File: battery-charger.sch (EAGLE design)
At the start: 9 parts, among them J2 10118192-0001LF, U1 MCP73831T-2DCI/OT

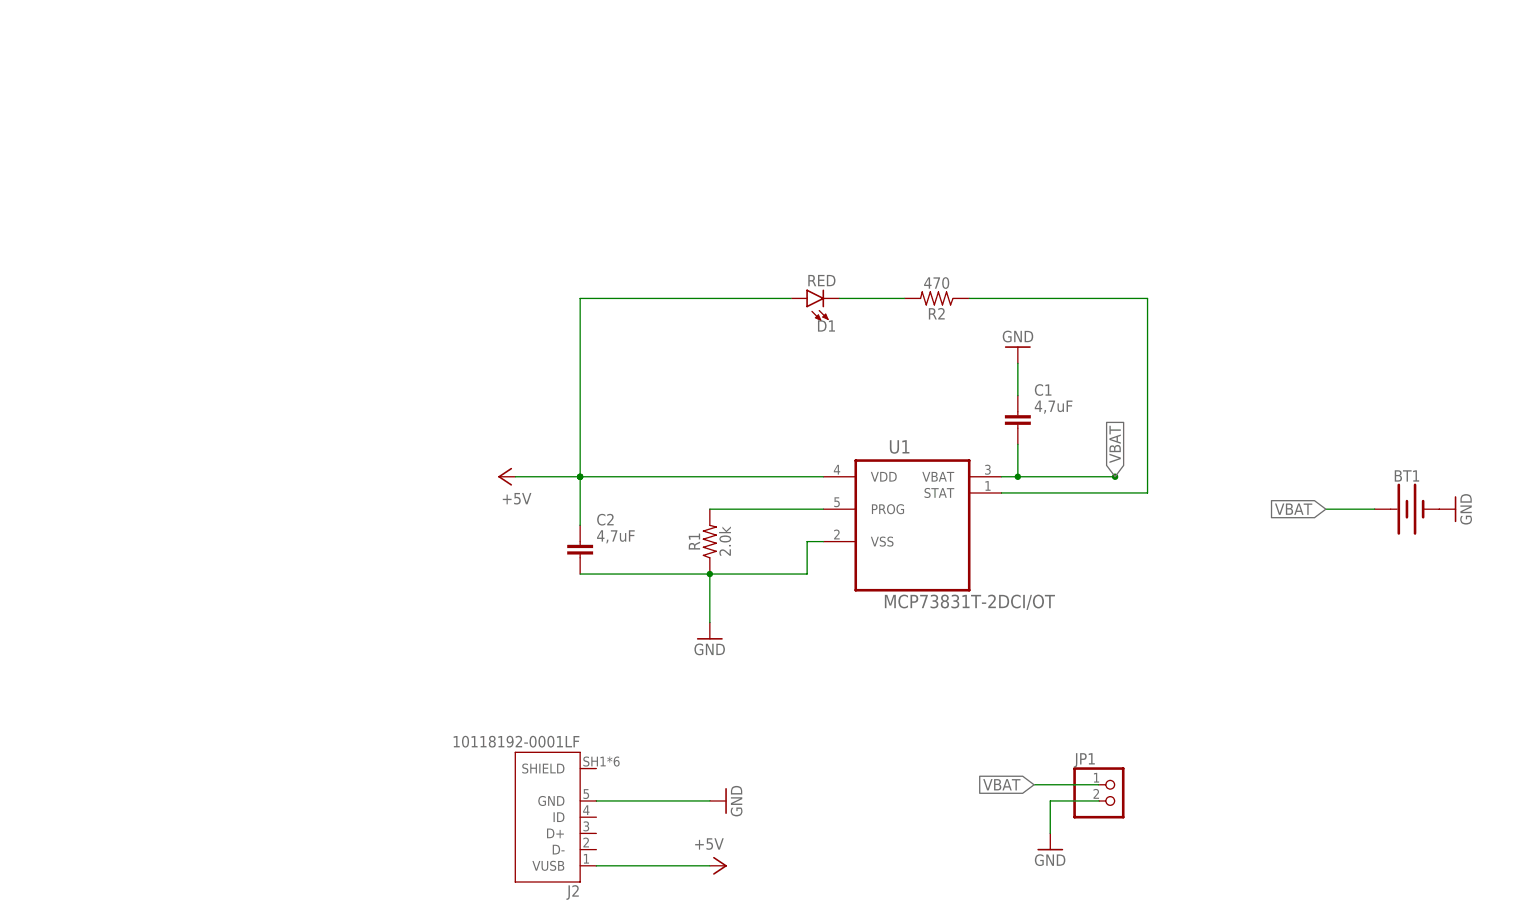
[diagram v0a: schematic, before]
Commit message: add under charge protection
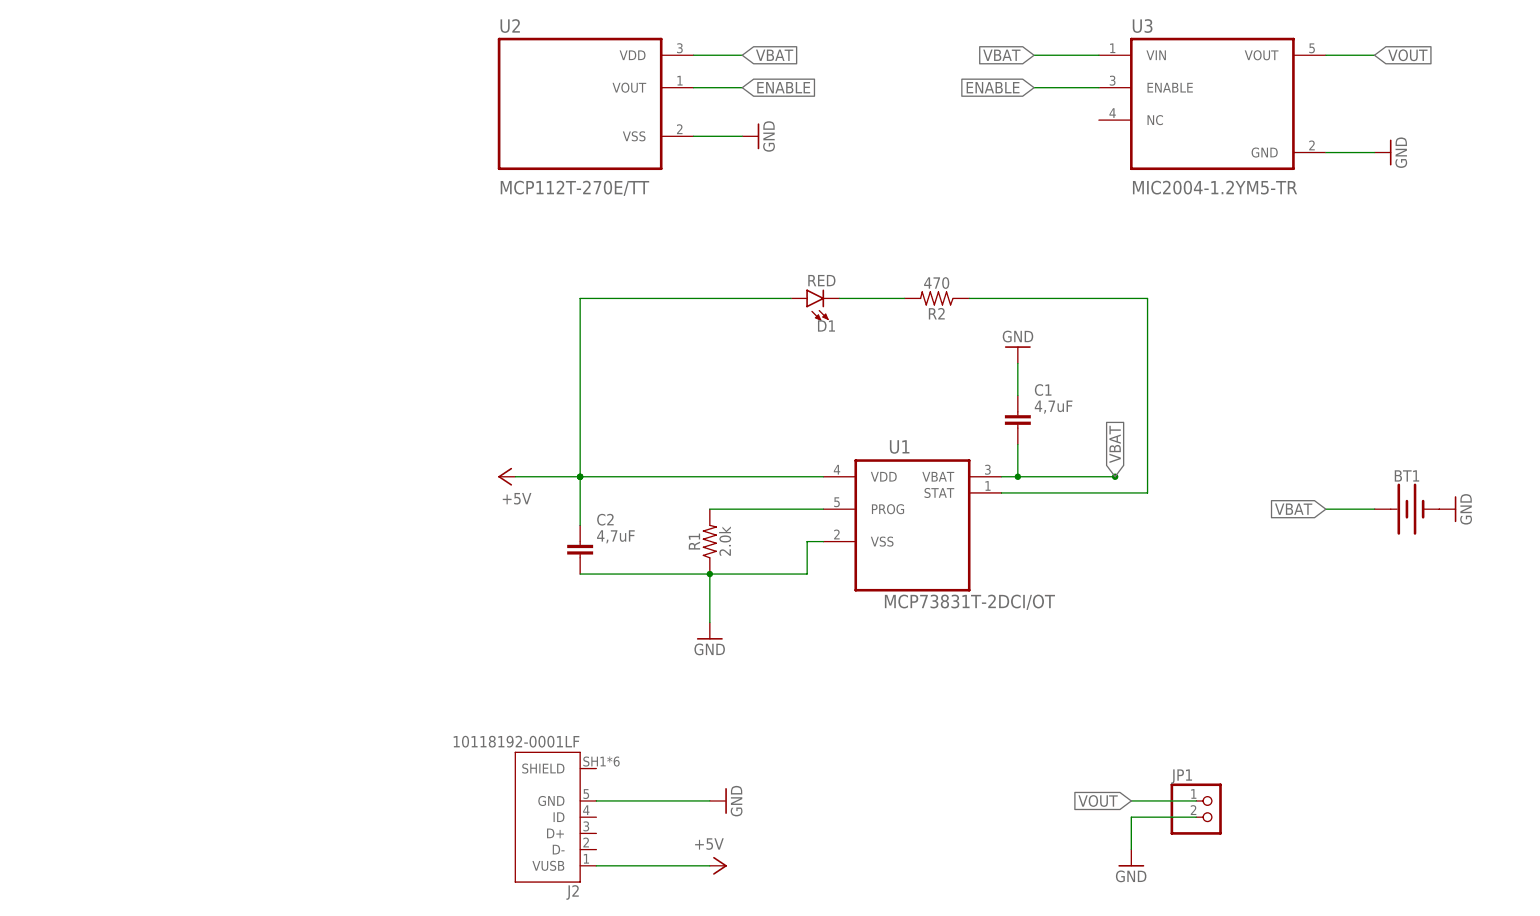
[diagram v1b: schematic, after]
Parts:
- added U2: MCP112T-270E/TT, MCP112T-270E_TT:MCP112T-270E/TT
- added U3: MIC2004-1.2YM5-TR, MIC2004-1.2YM5-TR:MIC2004-1.2YM5-TR
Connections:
- new net ENABLE: U2.VOUT, U3.ENABLE
- new net VOUT: JP1.1, U3.VOUT
- net GND: now also U2.VSS, U3.GND
- net VBAT: now also U2.VDD, U3.VIN; no longer JP1.1
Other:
- moved on the sheet: JP1
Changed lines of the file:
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@@
 <parts>
 <part name="U1" library="MCP73831T-2DCI_OT" deviceset="MCP73831T-2DCI/OT" device=""/>
-<part name="JP1" library="pinhead" library_urn="urn:adsk.eagle:library:325" deviceset="PINHD-1X2" device="" package3d_urn="urn:adsk.eagle:package:22435/2"/>
 <part name="R1" library="SparkFun-Resistors" library_urn="urn:adsk.eagle:library:532" deviceset="2.0KOHM" device="-0603-1/10W-5%" package3d_urn="urn:adsk.eagle:package:39650/1" value="2.0k"/>
 <part name="R2" library="SparkFun-Resistors" library_urn="urn:adsk.eagle:library:532" deviceset="470OHM" device="-0603-1/10W-1%" package3d_urn="urn:adsk.eagle:package:39650/1" value="470"/>
@@
 <part name="GND5" library="supply1" library_urn="urn:adsk.eagle:library:371" deviceset="GND" device=""/>
 <part name="J2" library="10118192-0001LF" deviceset="10118192-0001LF" device=""/>
+<part name="U2" library="MCP112T-270E_TT" deviceset="MCP112T-270E/TT" device=""/>
+<part name="GND6" library="supply1" library_urn="urn:adsk.eagle:library:371" deviceset="GND" device=""/>
+<part name="U3" library="MIC2004-1.2YM5-TR" deviceset="MIC2004-1.2YM5-TR" device=""/>
+<part name="GND7" library="supply1" library_urn="urn:adsk.eagle:library:371" deviceset="GND" device=""/>
+<part name="JP1" library="pinhead" library_urn="urn:adsk.eagle:library:325" deviceset="PINHD-1X2" device="" package3d_urn="urn:adsk.eagle:package:22435/2"/>
 </parts>
 <sheets>
@@
 <attribute name="VALUE" x="100.832059375" y="45.4502" size="2.08491875" layer="96" ratio="10" rot="SR0"/>
 </instance>
-<instance part="JP1" gate="G$1" x="137.16" y="15.24" smashed="yes">
-<attribute name="NAME" x="130.81" y="20.955" size="1.778" layer="95"/>
-<attribute name="VALUE" x="130.81" y="10.16" size="1.778" layer="96"/>
-</instance>
 <instance part="R1" gate="G$1" x="73.66" y="55.88" smashed="yes" rot="R90">
 <attribute name="NAME" x="72.136" y="55.88" size="1.778" layer="95" font="vector" rot="R90" align="bottom-center"/>
@@
 <attribute name="VALUE" x="124.46" y="88.9" size="1.778" layer="96" rot="R180"/>
 </instance>
-<instance part="GND4" gate="1" x="127" y="7.62" smashed="yes">
-<attribute name="VALUE" x="124.46" y="5.08" size="1.778" layer="96"/>
+<instance part="GND4" gate="1" x="139.7" y="5.08" smashed="yes">
+<attribute name="VALUE" x="137.16" y="2.54" size="1.778" layer="96"/>
 </instance>
 <instance part="BT1" gate="G$1" x="182.88" y="60.96" smashed="yes">
@@
 <attribute name="NAME" x="53.34618125" y="2.019" size="1.780159375" layer="95" rot="R180"/>
 <attribute name="VALUE" x="53.348209375" y="25.4205" size="1.78086875" layer="96" rot="R180"/>
+</instance>
+<instance part="U2" gate="G$1" x="53.34" y="124.46" smashed="yes">
+<attribute name="NAME" x="40.64" y="135.62" size="2.0828" layer="95" ratio="10" rot="SR0"/>
+<attribute name="VALUE" x="40.64" y="110.3" size="2.0828" layer="96" ratio="10" rot="SR0"/>
+</instance>
+<instance part="GND6" gate="1" x="81.28" y="119.38" smashed="yes" rot="R90">
+<attribute name="VALUE" x="83.82" y="116.84" size="1.778" layer="96" rot="R90"/>
+</instance>
+<instance part="U3" gate="G$1" x="152.4" y="124.46" smashed="yes">
+<attribute name="NAME" x="139.7" y="135.62" size="2.0828" layer="95" ratio="10" rot="SR0"/>
+<attribute name="VALUE" x="139.7" y="110.3" size="2.0828" layer="96" ratio="10" rot="SR0"/>
+</instance>
+<instance part="GND7" gate="1" x="180.34" y="116.84" smashed="yes" rot="R90">
+<attribute name="VALUE" x="182.88" y="114.3" size="1.778" layer="96" rot="R90"/>
+</instance>
+<instance part="JP1" gate="G$1" x="152.4" y="12.7" smashed="yes">
+<attribute name="NAME" x="146.05" y="18.415" size="1.778" layer="95"/>
+<attribute name="VALUE" x="146.05" y="7.62" size="1.778" layer="96"/>
 </instance>
 </instances>
@@
 </segment>
 <segment>
-<pinref part="JP1" gate="G$1" pin="2"/>
-<wire x1="134.62" y1="15.24" x2="127" y2="15.24" width="0.1524" layer="91"/>
-<wire x1="127" y1="15.24" x2="127" y2="10.16" width="0.1524" layer="91"/>
-<pinref part="GND4" gate="1" pin="GND"/>
-</segment>
-<segment>
 <pinref part="BT1" gate="G$1" pin="-"/>
 <pinref part="GND5" gate="1" pin="GND"/>
@@
 <pinref part="GND1" gate="1" pin="GND"/>
 <wire x1="55.88" y1="15.24" x2="73.66" y2="15.24" width="0.1524" layer="91"/>
+</segment>
+<segment>
+<pinref part="GND4" gate="1" pin="GND"/>
+<wire x1="149.86" y1="12.7" x2="139.7" y2="12.7" width="0.1524" layer="91"/>
+<wire x1="139.7" y1="12.7" x2="139.7" y2="7.62" width="0.1524" layer="91"/>
+<pinref part="JP1" gate="G$1" pin="2"/>
+</segment>
+<segment>
+<pinref part="U2" gate="G$1" pin="VSS"/>
+<wire x1="71.12" y1="119.38" x2="78.74" y2="119.38" width="0.1524" layer="91"/>
+<pinref part="GND6" gate="1" pin="GND"/>
+</segment>
+<segment>
+<pinref part="U3" gate="G$1" pin="GND"/>
+<wire x1="170.18" y1="116.84" x2="177.8" y2="116.84" width="0.1524" layer="91"/>
+<pinref part="GND7" gate="1" pin="GND"/>
 </segment>
 </net>
@@
 </segment>
 <segment>
-<pinref part="JP1" gate="G$1" pin="1"/>
-<wire x1="134.62" y1="17.78" x2="124.46" y2="17.78" width="0.1524" layer="91"/>
-<label x="124.46" y="17.78" size="1.778" layer="95" rot="R180" xref="yes"/>
-</segment>
-<segment>
 <pinref part="BT1" gate="G$1" pin="+"/>
 <wire x1="177.8" y1="60.96" x2="170.18" y2="60.96" width="0.1524" layer="91"/>
 <label x="170.18" y="60.96" size="1.778" layer="95" rot="R180" xref="yes"/>
 </segment>
-</net>
+<segment>
+<pinref part="U2" gate="G$1" pin="VDD"/>
+<wire x1="71.12" y1="132.08" x2="78.74" y2="132.08" width="0.1524" layer="91"/>
+<label x="78.74" y="132.08" size="1.778" layer="95" xref="yes"/>
+</segment>
+<segment>
+<pinref part="U3" gate="G$1" pin="VIN"/>
+<wire x1="134.62" y1="132.08" x2="124.46" y2="132.08" width="0.1524" layer="91"/>
+<label x="124.46" y="132.08" size="1.778" layer="95" rot="R180" xref="yes"/>
+</segment>
+</net>
+<net name="ENABLE" class="0">
+<segment>
+<pinref part="U3" gate="G$1" pin="ENABLE"/>
+<wire x1="134.62" y1="127" x2="124.46" y2="127" width="0.1524" layer="91"/>
+<label x="124.46" y="127" size="1.778" layer="95" rot="R180" xref="yes"/>
+</segment>
+<segment>
+<pinref part="U2" gate="G$1" pin="VOUT"/>
+<wire x1="71.12" y1="127" x2="78.74" y2="127" width="0.1524" layer="91"/>
+<label x="78.74" y="127" size="1.778" layer="95" xref="yes"/>
+</segment>
+</net>
+<net name="VOUT" class="0">
+<segment>
+<pinref part="U3" gate="G$1" pin="VOUT"/>
+<wire x1="170.18" y1="132.08" x2="177.8" y2="132.08" width="0.1524" layer="91"/>
+<label x="177.8" y="132.08" size="1.778" layer="95" xref="yes"/>
+</segment>
+<segment>
+<wire x1="149.86" y1="15.24" x2="139.7" y2="15.24" width="0.1524" layer="91"/>
+<label x="139.7" y="15.24" size="1.778" layer="95" rot="R180" xref="yes"/>
+<pinref part="JP1" gate="G$1" pin="1"/>
+</segment>
+</net>

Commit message: add on / off switch to charger
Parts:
- added U$1: CHS-01TASMD, CHS-01TA:CHS-01TASMD
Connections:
- new net VBAT_SWITCH: U$1.SO, U2.VDD, U3.VIN
- net VBAT: now also U$1.S!; no longer U2.VDD, U3.VIN
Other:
- moved on the sheet: BT1
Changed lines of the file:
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@@
 <part name="GND7" library="supply1" library_urn="urn:adsk.eagle:library:371" deviceset="GND" device=""/>
 <part name="JP1" library="pinhead" library_urn="urn:adsk.eagle:library:325" deviceset="PINHD-1X2" device="" package3d_urn="urn:adsk.eagle:package:22435/2"/>
+<part name="U$1" library="CHS-01TA" deviceset="CHS-01TA" device="SMD"/>
 </parts>
 <sheets>
@@
 <attribute name="VALUE" x="137.16" y="2.54" size="1.778" layer="96"/>
 </instance>
-<instance part="BT1" gate="G$1" x="182.88" y="60.96" smashed="yes">
-<attribute name="NAME" x="182.88" y="65.278" size="1.778" layer="95" font="vector" align="bottom-center"/>
-<attribute name="VALUE" x="182.88" y="56.642" size="1.778" layer="96" font="vector" align="top-center"/>
-</instance>
-<instance part="GND5" gate="1" x="190.5" y="60.96" smashed="yes" rot="R90">
-<attribute name="VALUE" x="193.04" y="58.42" size="1.778" layer="96" rot="R90"/>
+<instance part="BT1" gate="G$1" x="185.42" y="48.26" smashed="yes">
+<attribute name="NAME" x="185.42" y="52.578" size="1.778" layer="95" font="vector" align="bottom-center"/>
+<attribute name="VALUE" x="185.42" y="43.942" size="1.778" layer="96" font="vector" align="top-center"/>
+</instance>
+<instance part="GND5" gate="1" x="198.12" y="48.26" smashed="yes" rot="R90">
+<attribute name="VALUE" x="200.66" y="45.72" size="1.778" layer="96" rot="R90"/>
 </instance>
 <instance part="J2" gate="G$1" x="48.26" y="12.7" smashed="yes" rot="R180">
@@
 <attribute name="VALUE" x="146.05" y="7.62" size="1.778" layer="96"/>
 </instance>
+<instance part="U$1" gate="G$1" x="127" y="30.48" smashed="yes"/>
 </instances>
 <busses>
@@
 <pinref part="BT1" gate="G$1" pin="-"/>
 <pinref part="GND5" gate="1" pin="GND"/>
+<wire x1="190.5" y1="48.26" x2="195.58" y2="48.26" width="0.1524" layer="91"/>
 </segment>
 <segment>
@@
 <segment>
 <pinref part="BT1" gate="G$1" pin="+"/>
-<wire x1="177.8" y1="60.96" x2="170.18" y2="60.96" width="0.1524" layer="91"/>
-<label x="170.18" y="60.96" size="1.778" layer="95" rot="R180" xref="yes"/>
-</segment>
+<wire x1="180.34" y1="48.26" x2="175.26" y2="48.26" width="0.1524" layer="91"/>
+<label x="175.26" y="48.26" size="1.778" layer="95" rot="R180" xref="yes"/>
+</segment>
+<segment>
+<pinref part="U$1" gate="G$1" pin="S!"/>
+<wire x1="124.46" y1="30.48" x2="119.38" y2="30.48" width="0.1524" layer="91"/>
+<label x="119.38" y="30.48" size="1.778" layer="95" rot="R180" xref="yes"/>
+</segment>
+</net>
+<net name="ENABLE" class="0">
+<segment>
+<pinref part="U3" gate="G$1" pin="ENABLE"/>
+<wire x1="134.62" y1="127" x2="124.46" y2="127" width="0.1524" layer="91"/>
+<label x="124.46" y="127" size="1.778" layer="95" rot="R180" xref="yes"/>
+</segment>
+<segment>
+<pinref part="U2" gate="G$1" pin="VOUT"/>
+<wire x1="71.12" y1="127" x2="78.74" y2="127" width="0.1524" layer="91"/>
+<label x="78.74" y="127" size="1.778" layer="95" xref="yes"/>
+</segment>
+</net>
+<net name="VOUT" class="0">
+<segment>
+<pinref part="U3" gate="G$1" pin="VOUT"/>
+<wire x1="170.18" y1="132.08" x2="177.8" y2="132.08" width="0.1524" layer="91"/>
+<label x="177.8" y="132.08" size="1.778" layer="95" xref="yes"/>
+</segment>
+<segment>
+<wire x1="149.86" y1="15.24" x2="139.7" y2="15.24" width="0.1524" layer="91"/>
+<label x="139.7" y="15.24" size="1.778" layer="95" rot="R180" xref="yes"/>
+<pinref part="JP1" gate="G$1" pin="1"/>
+</segment>
+</net>
+<net name="VBAT_SWITCH" class="0">
 <segment>
 <pinref part="U2" gate="G$1" pin="VDD"/>
@@
 <label x="124.46" y="132.08" size="1.778" layer="95" rot="R180" xref="yes"/>
 </segment>
-</net>
-<net name="ENABLE" class="0">
-<segment>
-<pinref part="U3" gate="G$1" pin="ENABLE"/>
-<wire x1="134.62" y1="127" x2="124.46" y2="127" width="0.1524" layer="91"/>
-<label x="124.46" y="127" size="1.778" layer="95" rot="R180" xref="yes"/>
-</segment>
-<segment>
-<pinref part="U2" gate="G$1" pin="VOUT"/>
-<wire x1="71.12" y1="127" x2="78.74" y2="127" width="0.1524" layer="91"/>
-<label x="78.74" y="127" size="1.778" layer="95" xref="yes"/>
-</segment>
-</net>
-<net name="VOUT" class="0">
-<segment>
-<pinref part="U3" gate="G$1" pin="VOUT"/>
-<wire x1="170.18" y1="132.08" x2="177.8" y2="132.08" width="0.1524" layer="91"/>
-<label x="177.8" y="132.08" size="1.778" layer="95" xref="yes"/>
-</segment>
-<segment>
-<wire x1="149.86" y1="15.24" x2="139.7" y2="15.24" width="0.1524" layer="91"/>
-<label x="139.7" y="15.24" size="1.778" layer="95" rot="R180" xref="yes"/>
-<pinref part="JP1" gate="G$1" pin="1"/>
-</segment>
-</net>
+<segment>
+<pinref part="U$1" gate="G$1" pin="SO"/>
+<wire x1="139.7" y1="30.48" x2="147.32" y2="30.48" width="0.1524" layer="91"/>
+<label x="147.32" y="30.48" size="1.778" layer="95" xref="yes"/>
+</segment>
+</net>

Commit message: finalize battery charger
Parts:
- removed JP1: (no value), pinhead:PINHD-1X2
- added C3, C4: 1uF, Capacitor:C_CHIP-1206(3216-METRIC)
- added JP2: (no value), pinhead:PINHD-1X3
- added SJ1: (no value), jumper:SJW
- added U4: MIC5504-3.3YM5-T5, MIC5504-3.3YM5-T5:MIC5504-3.3YM5-T5
- C1, C2: DIGIKEY_PART_NR (none) -> 1276-3107-1-ND
- D1: DIGIKEY_PART_NR (none) -> 732-4978-1-ND
- R1: DIGIKEY_PART_NR (none) -> RMCF0201FT2K00CT-ND
- R2: DIGIKEY_PART_NR (none) -> YAG2689CT-ND
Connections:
- removed net VOUT: JP1.1, U3.VOUT
- new net +3V3: C4.1, JP2.1, U4.VOUT
- new net VRAW: C3.1, JP2.2, SJ1.1, U3.VOUT, U4.EN, U4.VIN
- net GND: now also C3.2, C4.2, JP2.3, U4.GND; no longer JP1.2
- net VBAT_SWITCH: now also SJ1.2
